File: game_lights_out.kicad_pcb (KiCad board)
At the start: 2 copper layers, 171.2 x 136.9 mm, 95 parts, among them SW1 SW_MEC_5E, SW10 SW_MEC_5E, SW11 SW_MEC_5E, SW12 SW_MEC_5E, SW13 SW_MEC_5E, SW14 SW_MEC_5E, SW15 SW_MEC_5E, SW16 SW_MEC_5E, SW17 SW_MEC_5E, SW18 SW_MEC_5E, SW19 SW_MEC_5E, SW2 SW_MEC_5E, SW20 SW_MEC_5E, SW21 SW_MEC_5E, SW22 SW_MEC_5E, SW23 SW_MEC_5E, SW24 SW_MEC_5E, SW25 SW_MEC_5E, SW26 SW_MEC_5E, SW27 SW_MEC_5E, SW28 SW_MEC_5E, SW29 SW_MEC_5E, SW3 SW_MEC_5E, SW30 SW_MEC_5E, SW31 SW_MEC_5E, SW32 SW_MEC_5E, SW33 SW_MEC_5E, SW34 SW_MEC_5E, SW35 SW_MEC_5E, SW36 SW_MEC_5E, SW37 SW_MEC_5E, SW38 SW_MEC_5E, SW39 SW_MEC_5E, SW4 SW_MEC_5E, SW40 SW_MEC_5E, SW5 SW_MEC_5E, SW6 SW_MEC_5E, SW7 SW_MEC_5E, SW8 SW_MEC_5E, SW9 SW_MEC_5E, U1 ATmega328-P, U2 ULN2803A

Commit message: Added labels to programming pins and updated file format
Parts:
- D1, D10, D11, D12, D13, D14, D15, D16, D17, D18, D19, D2, D20, D21, D22, D23, D24, D25, D26, D27, D28, D29, D3, D30, D31, D32, D33, D34, D35, D36, D37, D38, D39, D4, D40, D5, D6, D7, D8, D9: footprint LED_THT:LED_D5.0mm_IRGrey -> LED_THT:LED_D5.0mm
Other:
- board text added: "GND"
- board text added: "MISO"
- board text added: "MOSI"
- board text added: "RST"
- board text added: "SCK"
- board text added: "VCC"

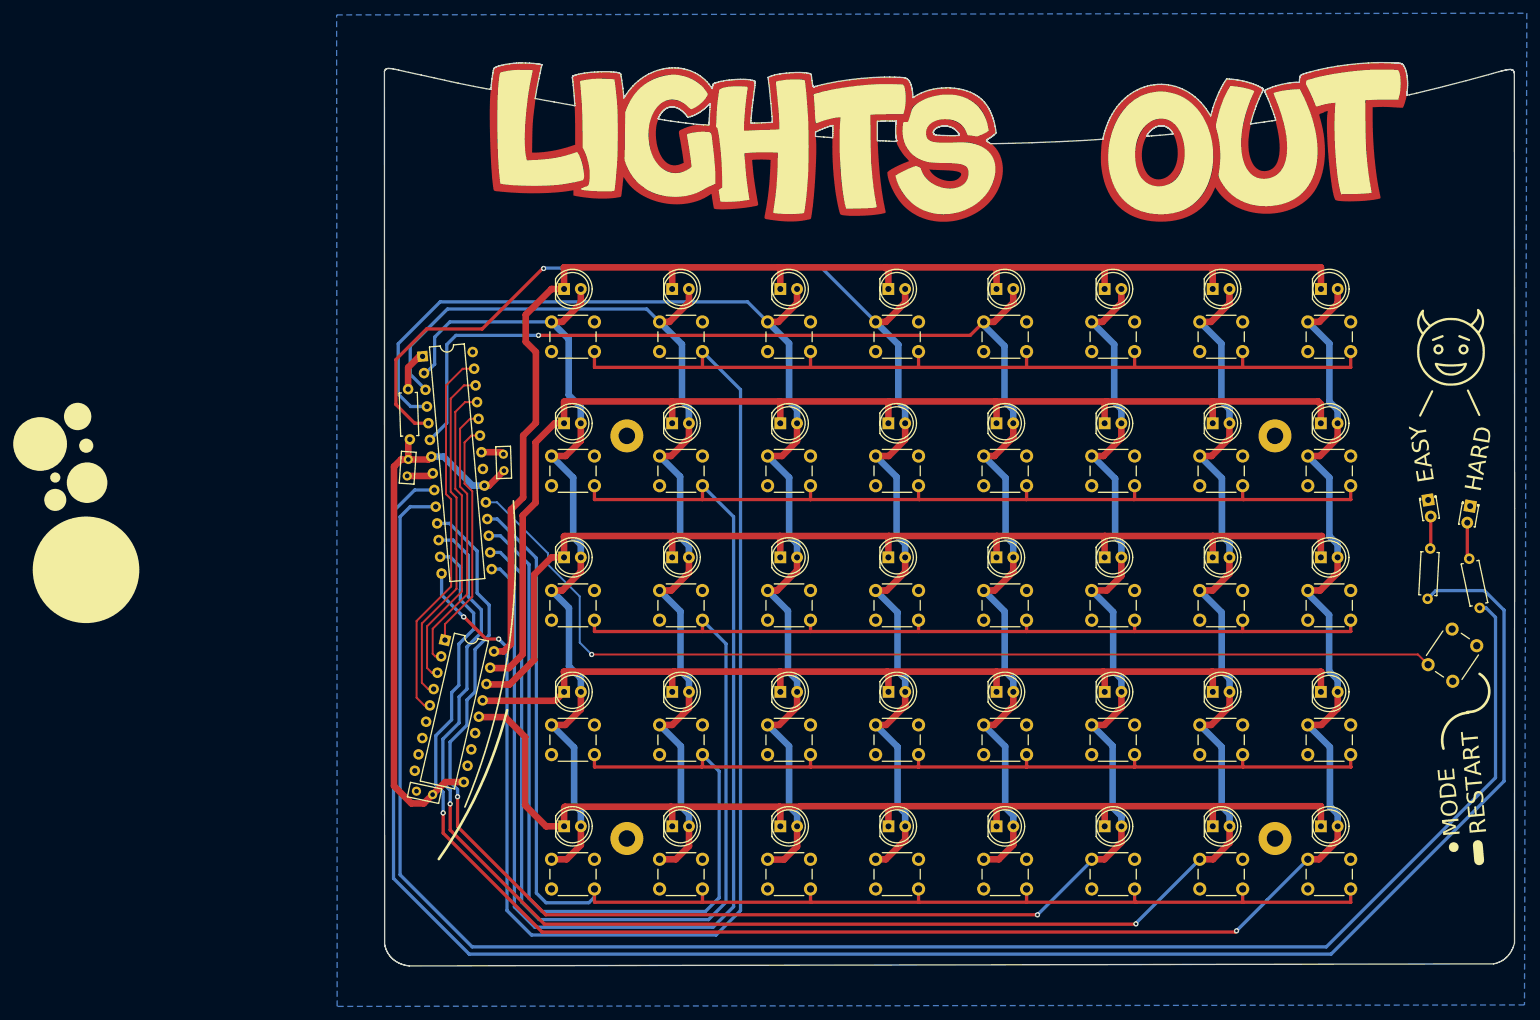
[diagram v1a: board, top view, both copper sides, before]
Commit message: Removed reset pin resistor
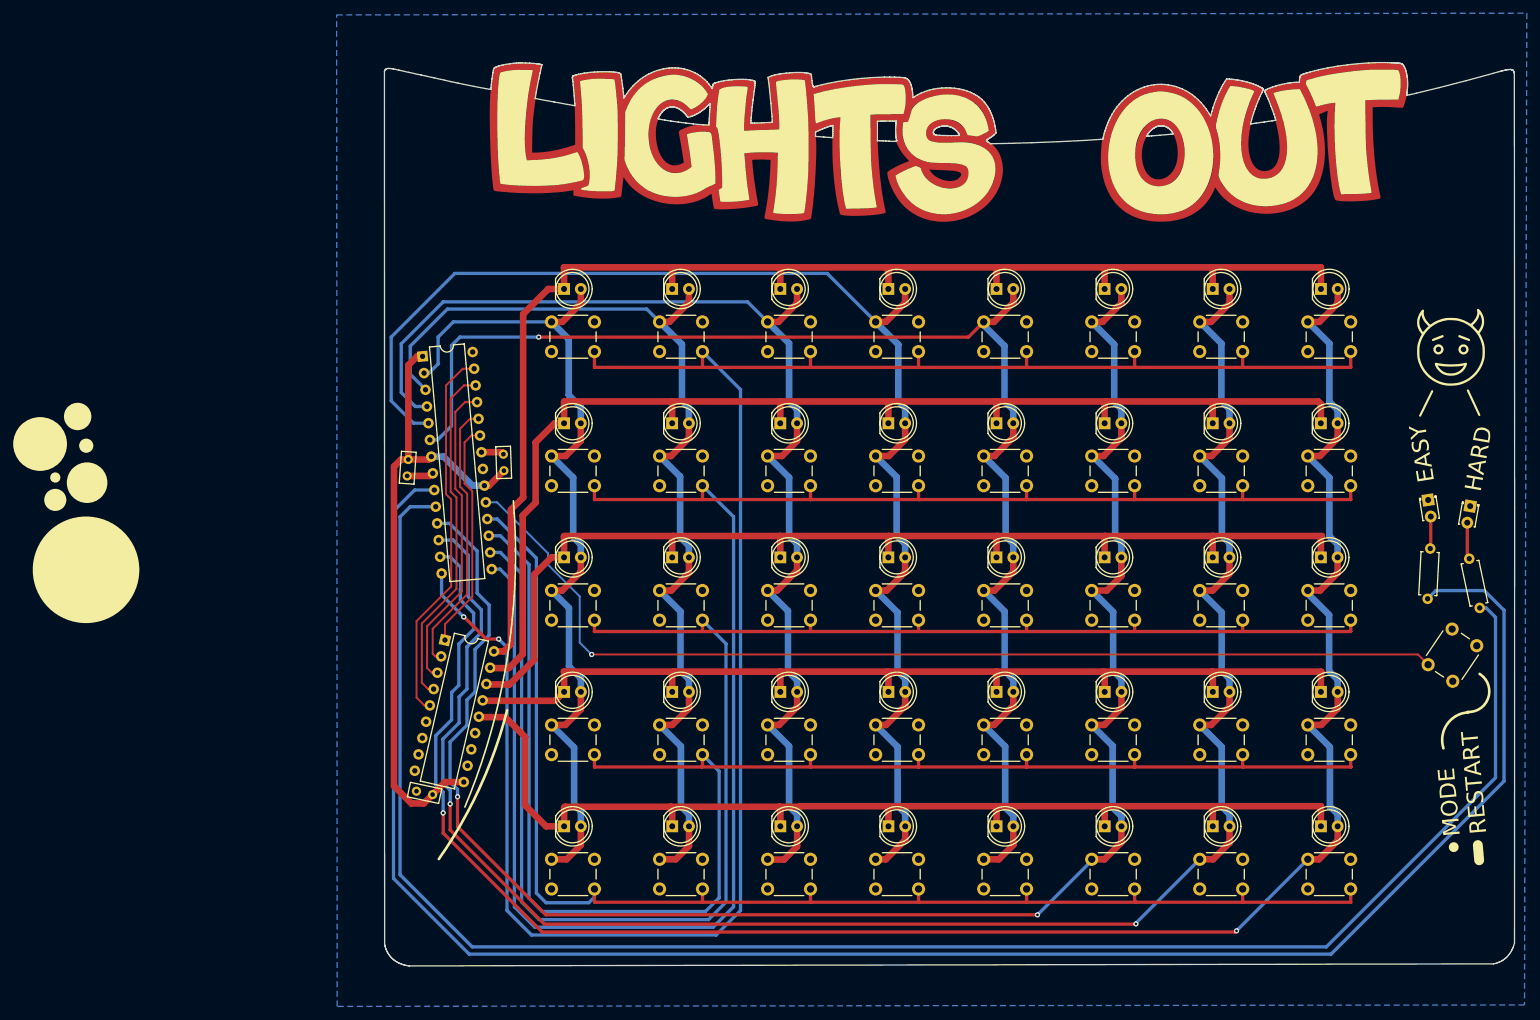
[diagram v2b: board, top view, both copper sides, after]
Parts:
- removed R1: 20K, Resistor_THT:R_Axial_DIN0207_L6.3mm_D2.5mm_P7.62mm_Horizontal
- removed REF** (x4): MountingHole_2.5mm_Pad, MountingHole:MountingHole_2.5mm_Pad
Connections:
- C1 pad 1: VCC -> RST
- C2 pad 1: VCC -> RST
- C3 pad 1: VCC -> RST
- U1 pad 20: VCC -> RST
- U1 pad 7: VCC -> RST
- U2 pad 10: VCC -> RST
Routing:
- net RST: track 6.16 -> 98.5 mm
- net VCC: track 84.6 -> 0.00 mm
- net C4: track 202.7 -> 205.2 mm, vias 1 -> 0
- net C3: track 181.3 -> 180.3 mm
- net R1: track 204.0 -> 203.0 mm

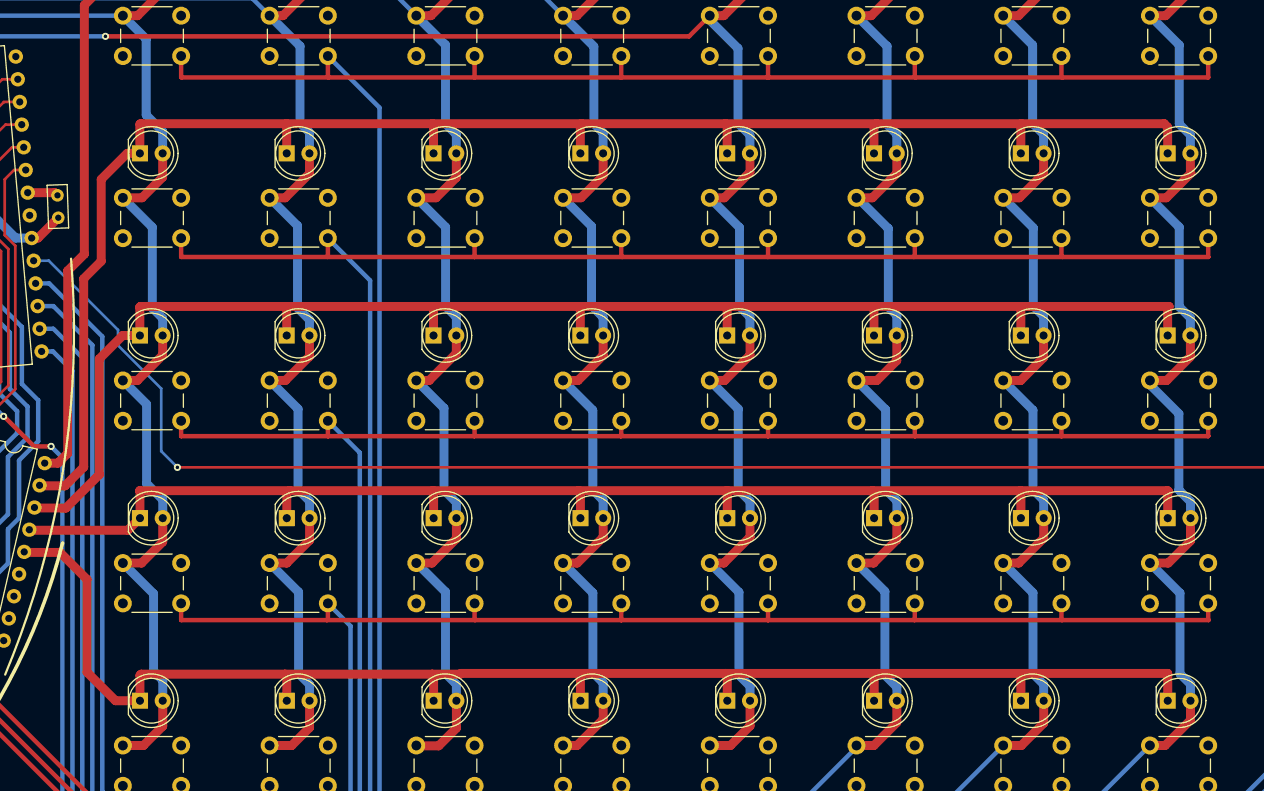
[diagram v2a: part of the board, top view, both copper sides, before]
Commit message: Added mounting holes
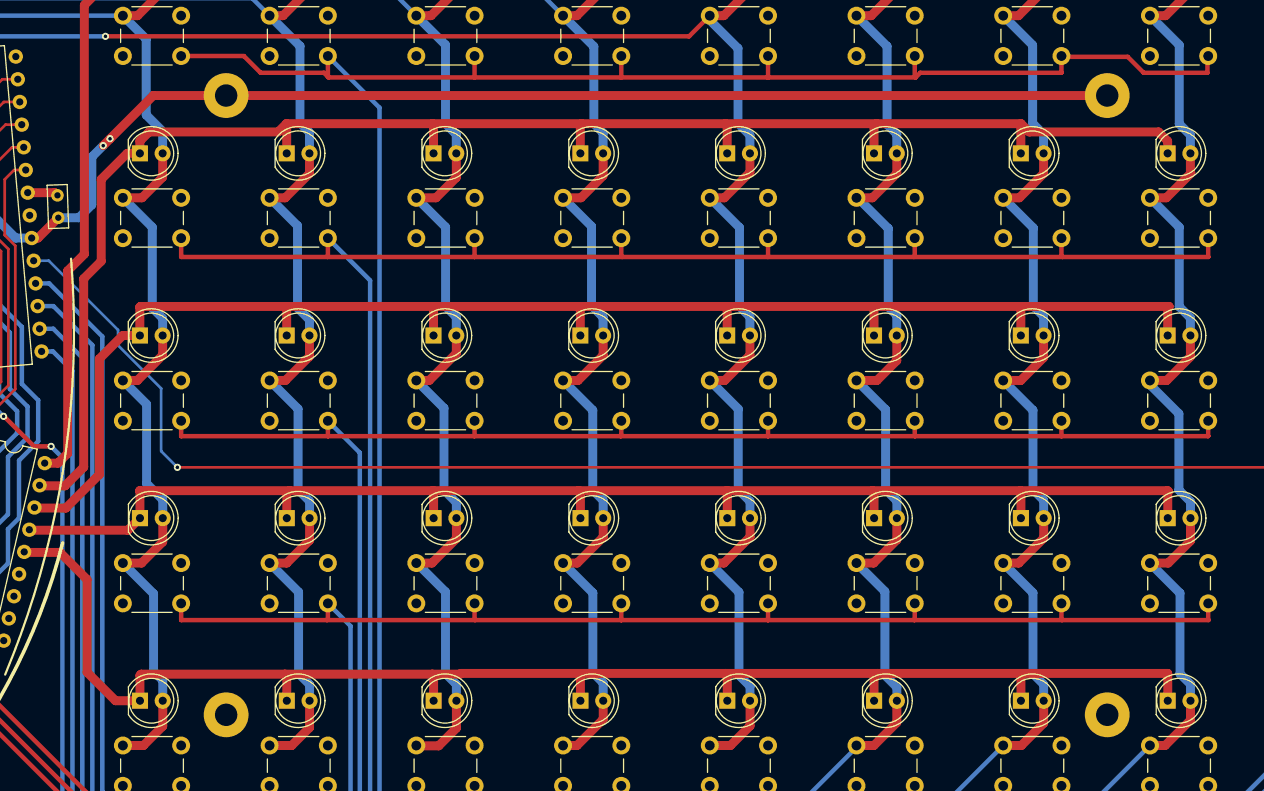
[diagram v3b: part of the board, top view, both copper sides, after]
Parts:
- added H1: MountingHole_Pad, MountingHole:MountingHole_2.5mm_Pad, F.Cu at (64.0, 144.5)
- added H2: MountingHole_Pad, MountingHole:MountingHole_2.5mm_Pad, F.Cu at (162.3, 144.5)
- added H3: MountingHole_Pad, MountingHole:MountingHole_2.5mm_Pad, F.Cu at (64.0, 75.4)
- added H4: MountingHole_Pad, MountingHole:MountingHole_2.5mm_Pad, F.Cu at (162.3, 75.4)
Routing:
- net RST: track 98.5 -> 226.5 mm, vias 0 -> 2
- net R2: track 185.4 -> 183.4 mm
- net SR1: track 315.7 -> 314.1 mm

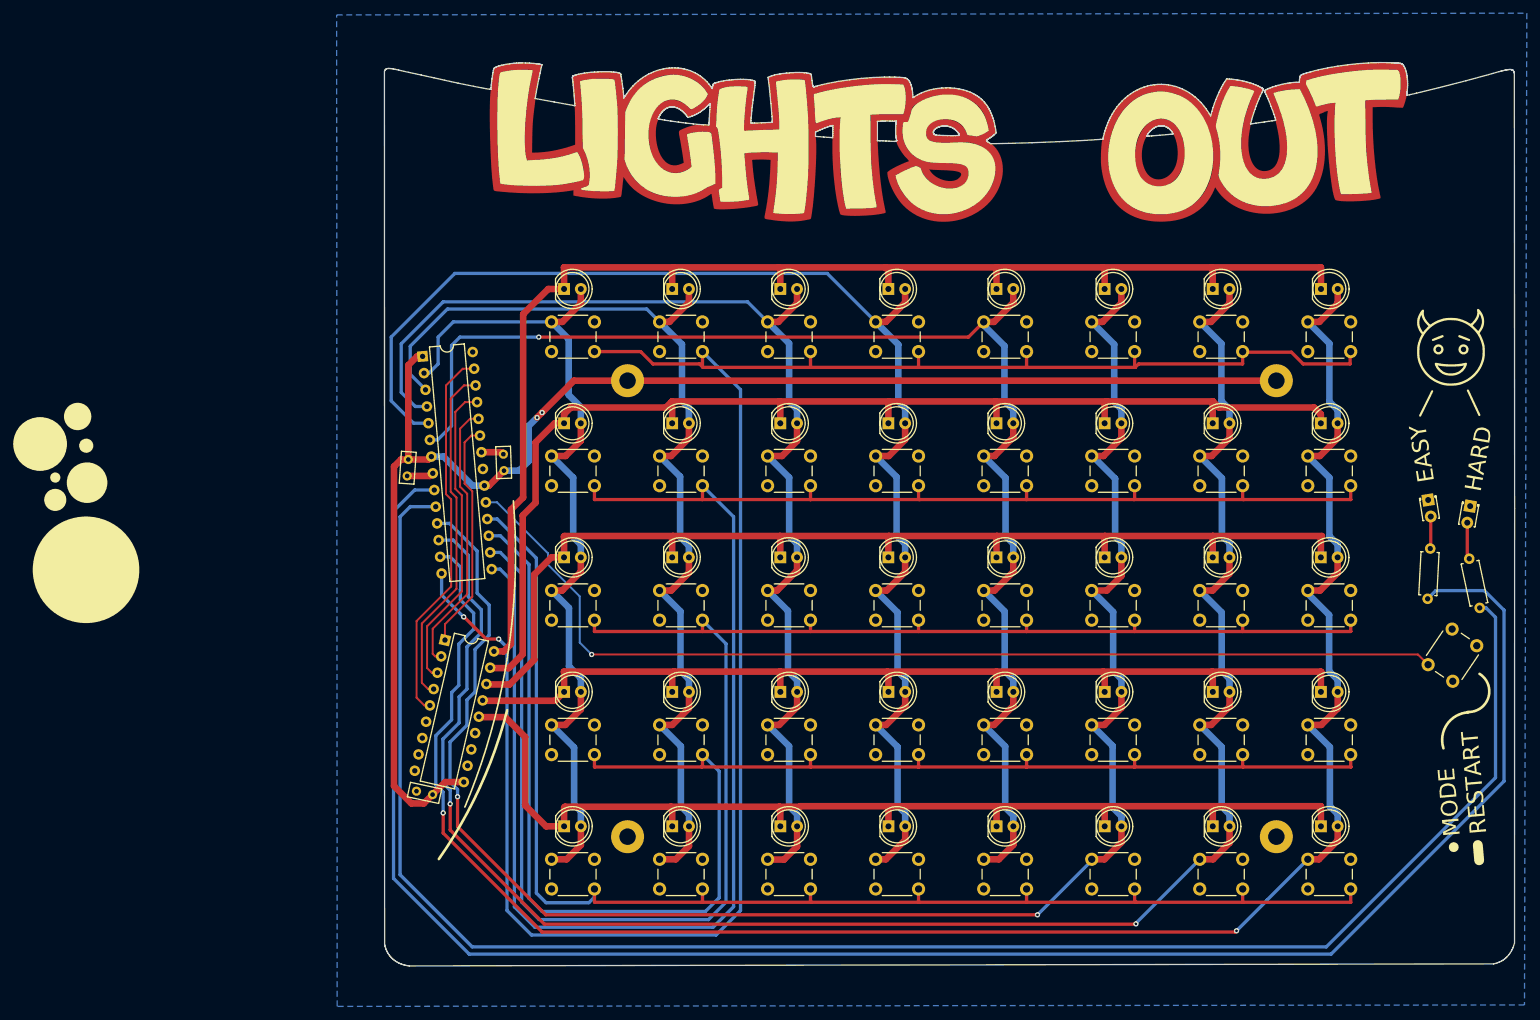
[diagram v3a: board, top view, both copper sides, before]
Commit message: Improved switch traces
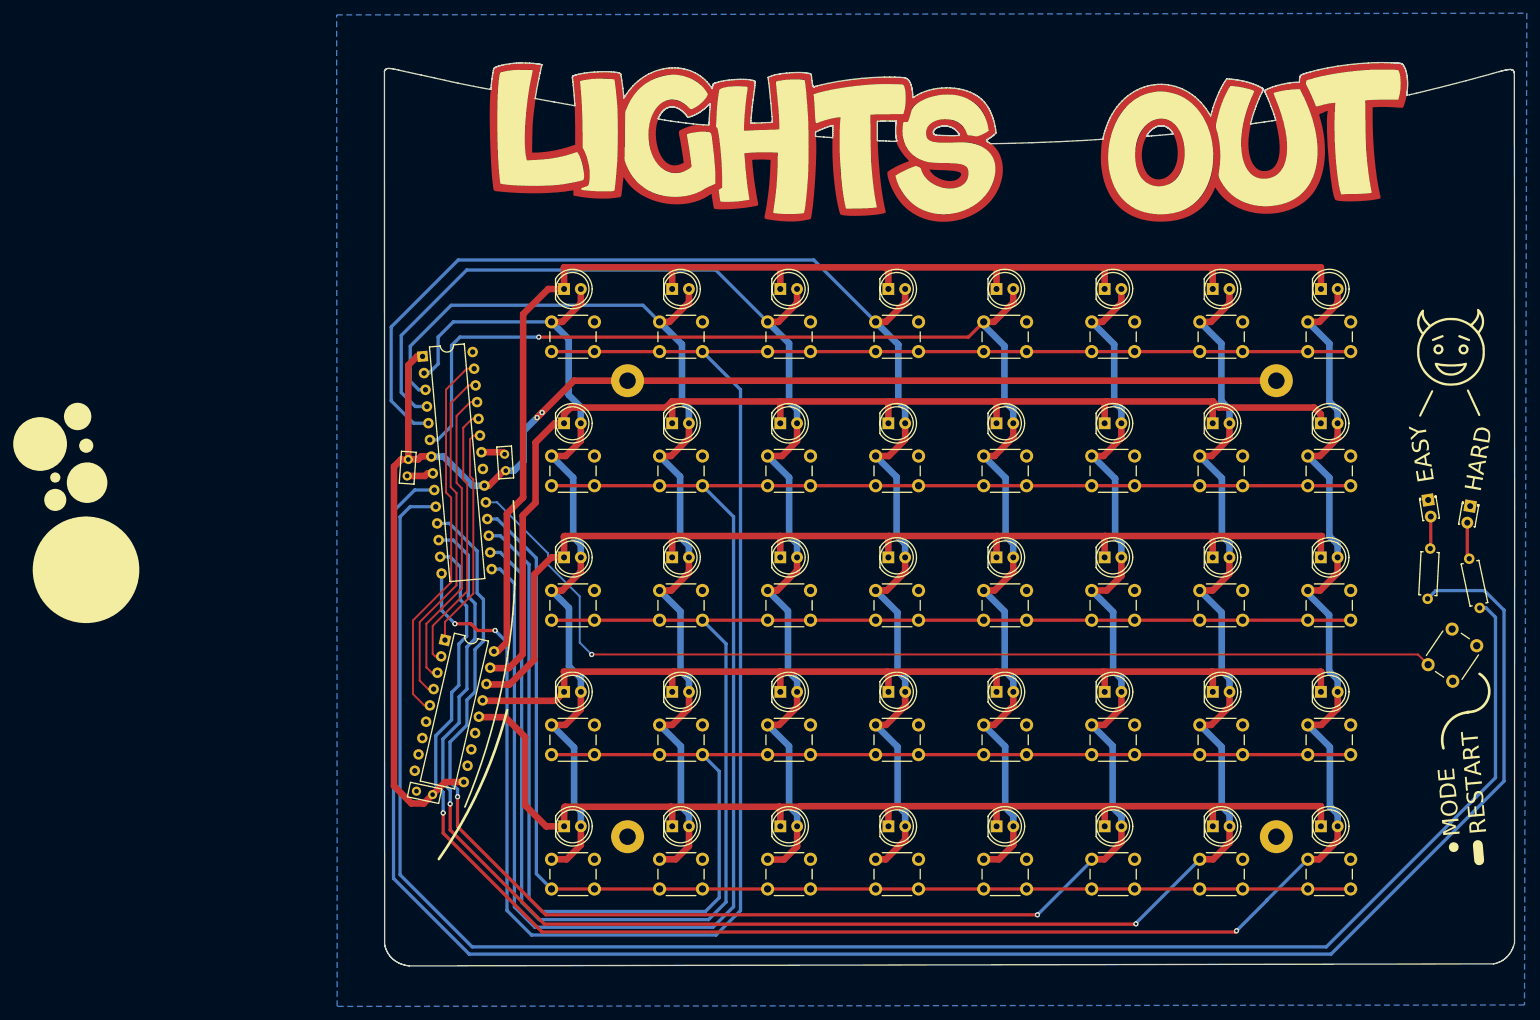
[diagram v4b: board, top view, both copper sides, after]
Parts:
- moved C1 0.27 mm to (45.6, 89.1), turned to 94 degrees
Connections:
- SW1 pad 3: unconnected-(SW1-K-Pad3) -> SR1
- SW10 pad 3: unconnected-(SW10-K-Pad3) -> SR2
- SW11 pad 3: unconnected-(SW11-K-Pad3) -> SR2
- SW12 pad 3: unconnected-(SW12-K-Pad3) -> SR2
- SW13 pad 3: unconnected-(SW13-K-Pad3) -> SR2
- SW14 pad 3: unconnected-(SW14-K-Pad3) -> SR2
- SW15 pad 3: unconnected-(SW15-K-Pad3) -> SR2
- SW16 pad 3: unconnected-(SW16-K-Pad3) -> SR2
- SW17 pad 3: unconnected-(SW17-K-Pad3) -> SR3
- SW18 pad 3: unconnected-(SW18-K-Pad3) -> SR3
- SW19 pad 3: unconnected-(SW19-K-Pad3) -> SR3
- SW2 pad 3: unconnected-(SW2-K-Pad3) -> SR1
- SW20 pad 3: unconnected-(SW20-K-Pad3) -> SR3
- SW21 pad 3: unconnected-(SW21-K-Pad3) -> SR3
- SW22 pad 3: unconnected-(SW22-K-Pad3) -> SR3
- SW23 pad 3: unconnected-(SW23-K-Pad3) -> SR3
- SW24 pad 3: unconnected-(SW24-K-Pad3) -> SR3
- SW25 pad 3: unconnected-(SW25-K-Pad3) -> SR4
- SW26 pad 3: unconnected-(SW26-K-Pad3) -> SR4
- SW27 pad 3: unconnected-(SW27-K-Pad3) -> SR4
- SW28 pad 3: unconnected-(SW28-K-Pad3) -> SR4
- SW29 pad 3: unconnected-(SW29-K-Pad3) -> SR4
- SW3 pad 3: unconnected-(SW3-K-Pad3) -> SR1
- SW30 pad 3: unconnected-(SW30-K-Pad3) -> SR4
- SW31 pad 3: unconnected-(SW31-K-Pad3) -> SR4
- SW32 pad 3: unconnected-(SW32-K-Pad3) -> SR4
- SW33 pad 3: unconnected-(SW33-K-Pad3) -> SR5
- SW34 pad 3: unconnected-(SW34-K-Pad3) -> SR5
- SW35 pad 3: unconnected-(SW35-K-Pad3) -> SR5
- SW36 pad 3: unconnected-(SW36-K-Pad3) -> SR5
- SW37 pad 3: unconnected-(SW37-K-Pad3) -> SR5
- SW38 pad 3: unconnected-(SW38-K-Pad3) -> SR5
- SW39 pad 3: unconnected-(SW39-K-Pad3) -> SR5
- SW4 pad 3: unconnected-(SW4-K-Pad3) -> SR1
- SW40 pad 3: unconnected-(SW40-K-Pad3) -> SR5
- SW5 pad 3: unconnected-(SW5-K-Pad3) -> SR1
- SW6 pad 3: unconnected-(SW6-K-Pad3) -> SR1
- SW7 pad 3: unconnected-(SW7-K-Pad3) -> SR1
- SW8 pad 3: unconnected-(SW8-K-Pad3) -> SR1
- SW9 pad 3: unconnected-(SW9-K-Pad3) -> SR2
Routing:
- net SR5: track 202.5 -> 182.1 mm
- net SR2: track 286.4 -> 275.9 mm
- net SR1: track 314.1 -> 305.0 mm
- net SR4: track 241.4 -> 232.8 mm
- net SR3: track 261.5 -> 254.3 mm
- net C3: track 180.3 -> 185.0 mm
- net C4: track 205.2 -> 207.7 mm
- net C2: track 157.0 -> 158.1 mm
- net C8: track 298.3 -> 297.4 mm
- net C7: track 283.0 -> 282.2 mm
- net Net-(U1-PC0): track 34.9 -> 34.2 mm
- net C6: track 267.6 -> 266.9 mm
- net RST: track 226.5 -> 227.2 mm
- net Net-(U1-PC1): track 41.6 -> 41.0 mm
- net Net-(U1-PC2): track 47.2 -> 46.6 mm
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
